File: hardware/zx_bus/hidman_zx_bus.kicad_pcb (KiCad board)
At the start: 2 copper layers, 99.1 x 40 mm, 31 parts, among them J1 X1A, J2 X1B, J3 UART, J4 Mini-DIN-6, J5 ISP, J6 Debug, J7 JTAG, J8 PS/2 External Bracket, U1 ATmega8A-A, U2 EPM3032ALC44, U3 AMS1117-3.3, U4 74LVC1G125DB

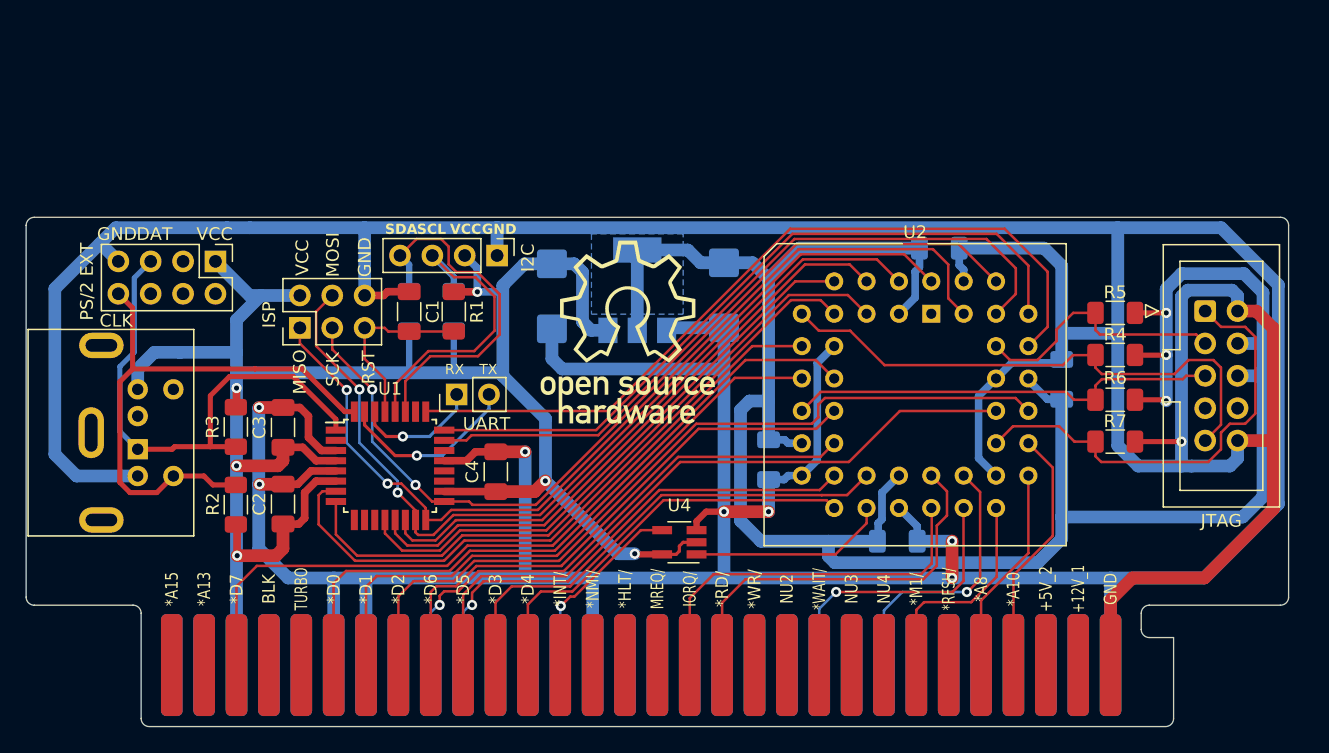
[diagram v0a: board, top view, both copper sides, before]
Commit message: Route ZX BUS card PCB.
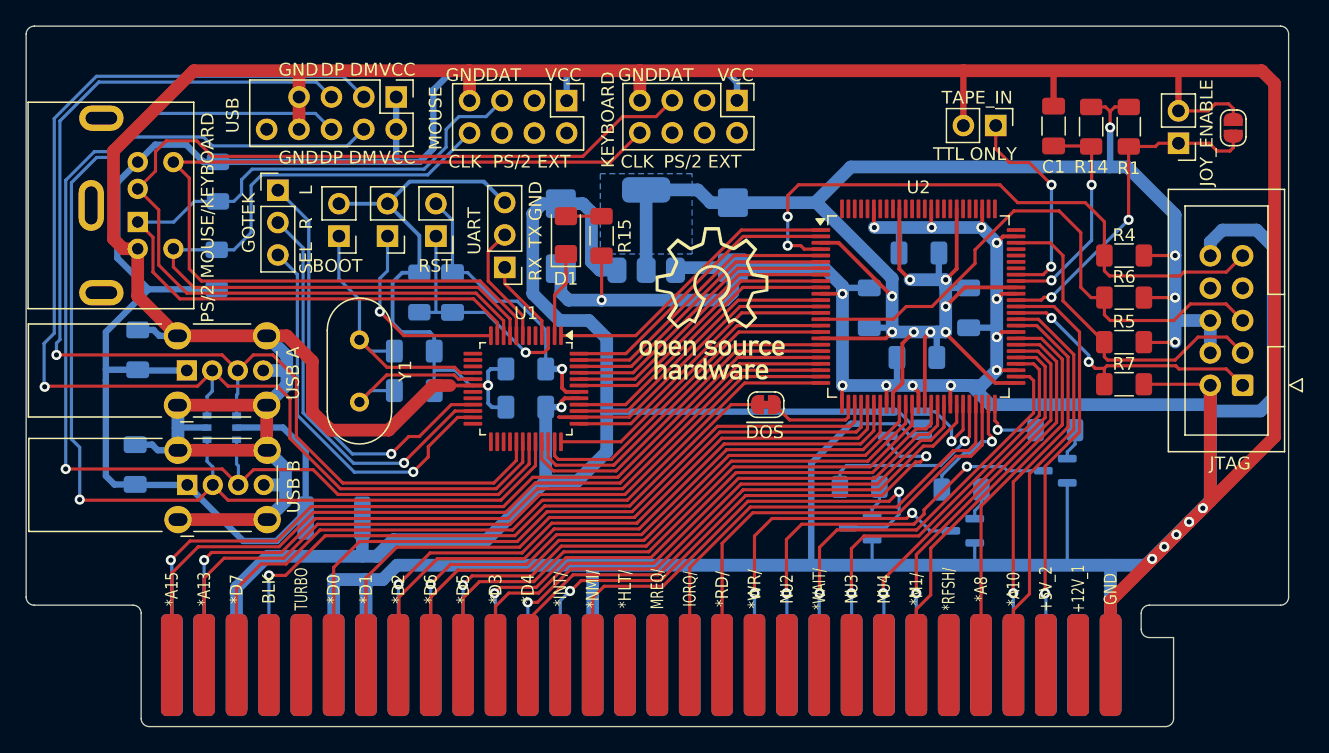
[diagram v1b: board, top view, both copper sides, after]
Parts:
- removed J6: Debug, Connector_PinHeader_2.54mm:PinHeader_1x04_P2.54mm_Vertical
- removed R8, R9: 2.2K, Resistor_SMD:R_1206_3216Metric_Pad1.30x1.75mm_HandSolder
- added C11: 0.1u, Capacitor_SMD:C_1206_3216Metric_Pad1.33x1.80mm_HandSolder, B.Cu at (112.6, 112.7)
- added C12: 0.1u, Capacitor_SMD:C_1206_3216Metric_Pad1.33x1.80mm_HandSolder, B.Cu at (116.5, 117.0)
- added C13: 0.1u, Capacitor_SMD:C_1206_3216Metric_Pad1.33x1.80mm_HandSolder, B.Cu at (112.4, 120.9)
- added C14: 0.1u, Capacitor_SMD:C_1206_3216Metric_Pad1.33x1.80mm_HandSolder, B.Cu at (108.7, 117.0)
- added D1: LED, LED_SMD:LED_1206_3216Metric_Pad1.42x1.75mm_HandSolder, F.Cu at (84.9, 111.3)
- added F2: Polyfuse, Fuse:Fuse_1812_4532Metric_Pad1.30x3.40mm_HandSolder, B.Cu at (66.7, 133.5)
- added J10: JOY_ENABLE, Connector_PinHeader_2.54mm:PinHeader_1x02_P2.54mm_Vertical, F.Cu at (133.0, 104.1)
- added J11: TAPE IN, Connector_PinHeader_2.54mm:PinHeader_1x02_P2.54mm_Vertical, F.Cu at (118.6, 102.7)
- added J12: USB EXT, Connector_PinHeader_2.54mm:PinHeader_2x05_P2.54mm_Vertical, F.Cu at (71.6, 100.5)
- added J13: PS/2 Mouse External Bracket, Connector_PinHeader_2.54mm:PinHeader_2x04_P2.54mm_Vertical, F.Cu at (85.0, 100.8)
- added J14: PS/2 Keyboard External Bracket, Connector_PinHeader_2.54mm:PinHeader_2x04_P2.54mm_Vertical, F.Cu at (98.3, 100.7)
- added J9: JTAG, Connector_IDC:IDC-Header_2x05_P2.54mm_Vertical, F.Cu at (138.0, 123.1)
- added JP1: SolderJumper_2_Bridged, Jumper:SolderJumper-2_P1.3mm_Bridged_RoundedPad1.0x1.5mm, F.Cu at (100.6, 124.6)
- added JP2: JOY_ENABLE, Jumper:SolderJumper-2_P1.3mm_Open_RoundedPad1.0x1.5mm, F.Cu at (137.3, 102.9)
- added Q1: BSS123, Package_TO_SOT_SMD:SOT-23, B.Cu at (116.0, 134.5)
- added Q2: BSS123, Package_TO_SOT_SMD:SOT-23, B.Cu at (108.0, 134.2)
- added Q3: BSS123, Package_TO_SOT_SMD:SOT-23, B.Cu at (123.3, 129.8)
- added R11: 1K, Resistor_SMD:R_1206_3216Metric_Pad1.30x1.75mm_HandSolder, B.Cu at (116.0, 131.3)
- added R12: 1K, Resistor_SMD:R_1206_3216Metric_Pad1.30x1.75mm_HandSolder, B.Cu at (108.0, 131.1)
- added R13: 1K, Resistor_SMD:R_1206_3216Metric_Pad1.30x1.75mm_HandSolder, B.Cu at (123.3, 126.6)
- added R14: 10K, Resistor_SMD:R_1206_3216Metric_Pad1.30x1.75mm_HandSolder, F.Cu at (126.1, 102.8)
- added R15: 1K, Resistor_SMD:R_1206_3216Metric_Pad1.30x1.75mm_HandSolder, F.Cu at (87.7, 111.4)
- added R16: 3.3K, Resistor_SMD:R_1206_3216Metric_Pad1.30x1.75mm_HandSolder, B.Cu at (57.5, 114.0)
- added SW1: RESET, Connector_PinHeader_2.54mm:PinHeader_1x02_P2.54mm_Vertical, F.Cu at (74.7, 111.4)
- added SW2: BOOT0, Connector_PinHeader_2.54mm:PinHeader_1x02_P2.54mm_Vertical, F.Cu at (67.1, 111.4)
- added SW3: BOOT1, Connector_PinHeader_2.54mm:PinHeader_1x02_P2.54mm_Vertical, F.Cu at (70.9, 111.4)
- added U6: IP4220CZ6, Package_SO:TSOP-6_1.65x3.05mm_P0.95mm, B.Cu at (57.9, 126.4)
- added Y1: 12MHz, Crystal:Crystal_HC49-4H_Vertical, F.Cu at (68.7, 124.4)
- C1: value 0.1u -> 0.1uF
- C2, C3: value 0.1u -> 22p; moved to B.Cu
- C4, U4: moved to B.Cu
- C5, C7, C8: value 0.1u -> 3.3u
- J3: footprint Connector_PinHeader_2.54mm:PinHeader_1x02_P2.54mm_Vertical -> Connector_PinHeader_2.54mm:PinHeader_1x03_P2.54mm_Vertical
- J4: value Mini-DIN-6 -> USB_A; footprint Connector_Mini-DIN_Female_6Pin:Connector_Mini-DIN_Female_6Pin_2rows -> Connector_USB:USB_A_Wuerth_614004134726_Horizontal
- J5: value ISP -> USB_A; footprint Connector_PinHeader_2.54mm:PinHeader_2x03_P2.54mm_Vertical -> Connector_USB:USB_A_Wuerth_614004134726_Horizontal
- J7: value JTAG -> Mouse / Key; footprint Connector_IDC:IDC-Header_2x05_P2.54mm_Vertical -> Connector_Mini-DIN_Female_6Pin:Connector_Mini-DIN_Female_6Pin_2rows
- J8: value PS/2 External Bracket -> GOTEK; footprint Connector_PinHeader_2.54mm:PinHeader_2x04_P2.54mm_Vertical -> Connector_PinHeader_2.54mm:PinHeader_1x03_P2.54mm_Vertical
- R1: value 2.2K -> 10K
- R2: value 4.7K -> 10K; moved to B.Cu
- R3: value 4.7K -> 3.3K; moved to B.Cu
- U1: value ATmega8A-A -> CH559L; footprint Package_QFP:TQFP-32_7x7mm_P0.8mm -> Package_QFP:LQFP-48_7x7mm_P0.5mm
- U2: value EPM3032ALC44 -> EPM3128ATC100; footprint Package_LCC:PLCC-44_THT-Socket -> Package_QFP:TQFP-100_14x14mm_P0.5mm
- moved J7 84.1 mm to (51.3, 110.3), turned to -90 degrees
- moved C7 60.1 mm to (51.1, 129.3), turned to 90 degrees
- moved R1 54.9 mm to (129.1, 102.8)
- moved C1 52.6 mm to (123.2, 102.7)
- moved C8 50.2 mm to (51.3, 120.3), turned to 90 degrees
- moved C5 42.1 mm to (81.8, 121.8), turned to 180 degrees
- moved C6 38.4 mm to (76.0, 115.8), turned to -90 degrees
- moved R2 22.0 mm to (73.4, 115.8), turned to 90 degrees
- moved U4 20.0 mm to (111.5, 126.1)
- moved R3 19.3 mm to (57.6, 107.1)
- moved C2 15.8 mm to (73.0, 120.4), turned to 0 degrees
- moved J5 15.2 mm to (55.2, 130.9), turned to 0 degrees
- moved U1 12.3 mm to (81.8, 123.3), turned to -90 degrees
- moved C3 10.7 mm to (73.0, 123.5), turned to 0 degrees
- moved J3 10.7 mm to (80.1, 113.8), turned to 180 degrees
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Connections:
- C1 pad 2: /RST -> /RST_IN
- C10 pad 1: /+3.3V -> +3.3V_CPLD
- C2 pad 1: VCC -> /P4_6
- C3 pad 1: VCC -> Net-(U1-P4.7/X0/SCK_)
- C4 pad 1: VCC -> +5V
- C5 pad 1: /+3.3V -> +3V3_MCU
- C6 pad 1: /+3.3V -> +3V3_MCU
- C6 pad 2: GND -> /RST
- C7 pad 1: /+3.3V -> +5V_FUSED
- C8 pad 1: /+3.3V -> +5V_FUSED
- C9 pad 1: VCC -> +5V
- J1 pad 3: VCC -> +5V
- J4 pad 1: /MDAT -> +5V_FUSED
- J4 pad 2: unconnected-(J4-Pad2) -> /DM_A
- J4 pad 3: GND -> /DP_A
- J4 pad 4: VCC -> GND
- J4 pad 5: /MCLK -> GND
- J5 pad 1: /DI4/MISO -> +5V_FUSED
- J5 pad 2: VCC -> /DM_B
- J5 pad 3: /DI5/SCK -> /DP_B
- J5 pad 4: /DI3/MOSI -> GND
- J5 pad 5: /RST -> GND
- J7 pad 1: /TCK -> /M_DAT
- J7 pad 2: GND -> /KEY_DAT
- J7 pad 3: /TDO -> GND
- J7 pad 4: /+3.3V -> +5V_FUSED
- J7 pad 5: /TMS -> /M_CLK
- J7 pad 6: /+3.3V -> /KEY_CLK
- J7 pad 7: unconnected-(J7-Pin_7-Pad7) -> (no net)
- J8 pad 1: VCC -> /LEFT
- J8 pad 2: unconnected-(J8-Pin_2-Pad2) -> /RIGHT
- J8 pad 3: unconnected-(J8-Pin_3-Pad3) -> /SELECT
- R1 pad 1: VCC -> +3.3V_CPLD
- R1 pad 2: /RST -> /JOY_ENABLE
- R2 pad 1: /MCLK -> /RST
- R2 pad 2: VCC -> GND
- R3 pad 1: /MDAT -> /M_DAT
- R3 pad 2: VCC -> +5V_FUSED
- R4 pad 2: /+3.3V -> +3.3V_CPLD
- R5 pad 2: /+3.3V -> +3.3V_CPLD
- R6 pad 2: /+3.3V -> +3.3V_CPLD
- U1 pad 1: /MDAT -> /JOY
- U1 pad 10: unconnected-(U1-PD6-Pad10) -> /KEY_DAT
- U1 pad 11: unconnected-(U1-PD7-Pad11) -> /M_DAT
- U1 pad 12: /DI0 -> /P3_6
- U1 pad 13: /DI1 -> /P3_7
- U1 pad 14: /DI2 -> /P4_3
- U1 pad 15: /DI3/MOSI -> /P4_2
- U1 pad 16: /DI4/MISO -> /P4_6
- U1 pad 17: /DI5/SCK -> Net-(U1-P4.7/X0/SCK_)
- U1 pad 18: VCC -> GND
- U1 pad 19: unconnected-(U1-ADC6-Pad19) -> /P4_1
- U1 pad 2: unconnected-(U1-PD4-Pad2) -> /P1_7
- U1 pad 20: unconnected-(U1-AREF-Pad20) -> /P4_0
- U1 pad 21: GND -> /LEFT
- U1 pad 22: unconnected-(U1-ADC7-Pad22) -> /RIGHT
- U1 pad 23: /MX -> /SELECT
- U1 pad 24: /MY -> /P2_3
- U1 pad 25: /MKEY -> /P2_4
- U1 pad 26: unconnected-(U1-PC3-Pad26) -> /P2_5
- U1 pad 27: /SDA -> /P2_6
- U1 pad 28: /SCL -> /P2_7
- U1 pad 29: /RST -> /DP_A
- U1 pad 3: GND -> /RST
- U1 pad 30: /RX -> /DM_A
- U1 pad 31: /TX -> /DP_B
- U1 pad 32: /MCLK -> /DM_B
- U1 pad 4: VCC -> /RX
- U1 pad 5: GND -> /P4_5
- U1 pad 6: VCC -> /P4_4
- U1 pad 7: /DI6 -> /TX
- U1 pad 8: /DI7 -> /KEY_CLK
- U1 pad 9: unconnected-(U1-PD5-Pad9) -> /M_CLK
- U2 pad 1: unconnected-(U2A-~{GCLR}-Pad1) -> /JOY
- U2 pad 10: GND -> /DI0
- U2 pad 11: /*D1 -> GND
- U2 pad 12: /*D0 -> /DI1
- U2 pad 13: /TMS -> /DI2
- U2 pad 14: /*D6 -> /DI3
- U2 pad 15: /+3.3V -> /TMS
- U2 pad 16: /*A0 -> /DI4
- U2 pad 17: GND -> /DI5
- U2 pad 18: /*D4 -> +3.3V_CPLD
- U2 pad 19: /*A1 -> /DI6
- U2 pad 2: /DI2 -> /STROBE
- U2 pad 20: /IORQGE/ -> /DI7
- U2 pad 21: /*D3 -> /*A14
- U2 pad 22: GND -> /*A15
- U2 pad 23: /+3.3V -> /*A12
- U2 pad 24: /*IORQ/ -> /*A13
- U2 pad 25: /*RD/ -> /*D7
- U2 pad 26: /*A7 -> GND
- U2 pad 27: /*A5 -> /DOS_IN
- U2 pad 28: /*M1/ -> /*D0
- U2 pad 29: /*A8 -> /*D1
- U2 pad 3: /+3.3V -> +3.3V_CPLD
- U2 pad 30: GND -> /CLK
- U2 pad 31: /*A10 -> /*D2
- U2 pad 32: /TCK -> /*A0
- U2 pad 33: /*D2 -> GND
- U2 pad 34: /*D5 -> +3.3V_CPLD
- U2 pad 35: /+3.3V -> /*D6
- U2 pad 36: GND -> /*A1
- U2 pad 37: /MKEY -> /*D5
- U2 pad 38: /TDO -> GND
- U2 pad 39: /MY -> +3.3V_CPLD
- U2 pad 4: /DI1 -> /TDI
- U2 pad 40: /DI5/SCK -> /*A2
- U2 pad 41: /MX -> /*D3
- U2 pad 42: GND -> /*A3
- U2 pad 43: /DI4/MISO -> GND
- U2 pad 44: /DI3/MOSI -> /*D4
- U2 pad 5: /DI7 -> /SCLK
- U2 pad 6: /DI0 -> /DAT
- U2 pad 7: /TDI -> /MKEY
- U2 pad 8: /DI6 -> /MY
- U2 pad 9: /*D7 -> /MX
- U3 pad 2: /+3.3V -> +3.3V_CPLD
- U3 pad 3: VCC -> +5V
- U4 pad 2: VCC -> +5V
- U4 pad 5: VCC -> +5V
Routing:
- net /+3.3V: track 176.1 -> 0.00 mm, vias 3 -> 0
- net +3.3V_CPLD: track 0.00 -> 163.0 mm, vias 0 -> 12
- net VCC: track 160.8 -> 0.00 mm, vias 6 -> 0
- net +5V_FUSED: track 0.00 -> 132.2 mm
- net GND: track 505.7 -> 618.9 mm, vias 8 -> 19
- net +5V: track 0.00 -> 110.4 mm, vias 0 -> 1
- net /DM_A: track 0.00 -> 97.7 mm, vias 0 -> 1
- net /DM_B: track 0.00 -> 93.9 mm, vias 0 -> 1
- net /DP_A: track 0.00 -> 91.2 mm, vias 0 -> 1
- net /DP_B: track 0.00 -> 90.7 mm, vias 0 -> 1
- net /KEY_DAT: track 0.00 -> 83.5 mm
- net /KEY_CLK: track 0.00 -> 75.1 mm
- net /DI4/MISO: track 74.5 -> 0.00 mm, vias 2 -> 0
- net /DI3/MOSI: track 72.9 -> 0.00 mm, vias 2 -> 0
- net /DI5/SCK: track 71.1 -> 0.00 mm, vias 2 -> 0
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- added copper zone on B.Cu, net +3.3V_CPLD
- removed copper zone on B.Cu, net /+3.3V
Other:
- board size 99.1 x 40 mm -> 99.1 x 55 mm
- board text added: "BOOT"
- board text added: "DM"
- board text added: "DP"
- board text added: "GOTEK"
- board text added: "JOY_ENABLE"
- board text added: "KEYBOARD"
- board text added: "L"
- board text added: "MOUSE"
- board text added: "PS/2 MOUSE/KEYBOARD"
- board text added: "R"
- board text added: "SEL"
- board text added: "TAPE_IN"
- board text added: "TTL ONLY"
- board text added: "USB"
- board text added: "USB A"
- board text added: "USB B"
- board text added: "V.1.0"
- board text added: "ZX BUS USB / PS/2 Input Controller"
- board text added: "~{DOS}"
- board text removed: "I2C"
- board text removed: "ISP"
- board text removed: "MISO"
- board text removed: "MOSI"
- board text removed: "SCK"
- board text removed: "SCL"
- board text removed: "SDA"
- board text removed: "ZX BUS Kempston Mouse Controller"

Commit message: Remove BOOT1 switch from schematic. Correct LED polarity.
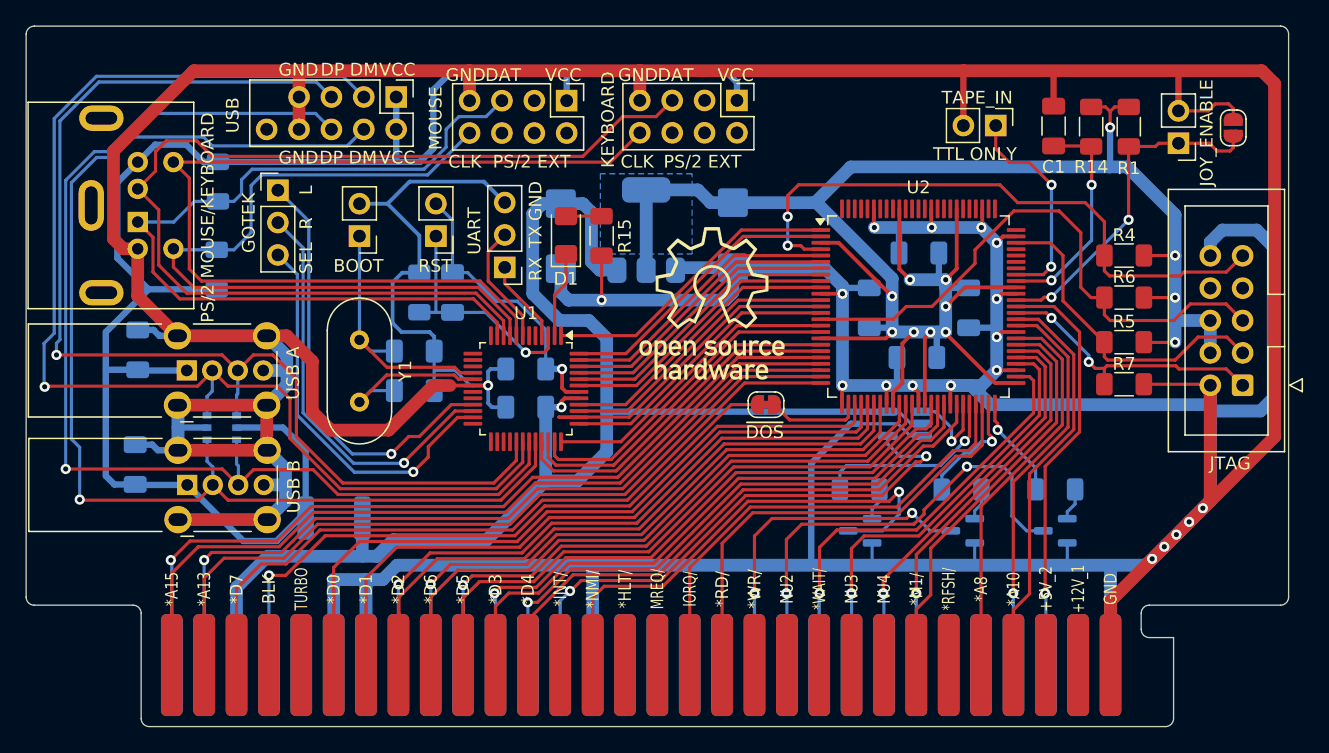
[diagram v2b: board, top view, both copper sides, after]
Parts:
- removed SW3: BOOT1, Connector_PinHeader_2.54mm:PinHeader_1x02_P2.54mm_Vertical
- moved Q3 4.71 mm to (123.3, 134.5)
- moved R13 4.65 mm to (123.3, 131.2)
- moved SW2 1.61 mm to (68.7, 111.4)
- moved Q2 0.25 mm to (108.0, 134.5)
- moved R12 0.20 mm to (108.0, 131.2)
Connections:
- D1 pad 1: /P1_7 -> Net-(D1-K)
- D1 pad 2: Net-(D1-A) -> /P1_7
- R15 pad 1: Net-(D1-A) -> Net-(D1-K)
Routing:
- net /P3_6: track 15.7 -> 0.00 mm, vias 1 -> 0
- net GND: track 618.9 -> 612.3 mm
- net /*RST/: track 32.7 -> 36.6 mm
- net /RST_OUT: track 5.09 -> 8.01 mm
- net Net-(D1-A): track 2.80 -> 0.00 mm
- net /P1_7: track 6.77 -> 9.57 mm
- net /P4_6: track 21.9 -> 21.2 mm

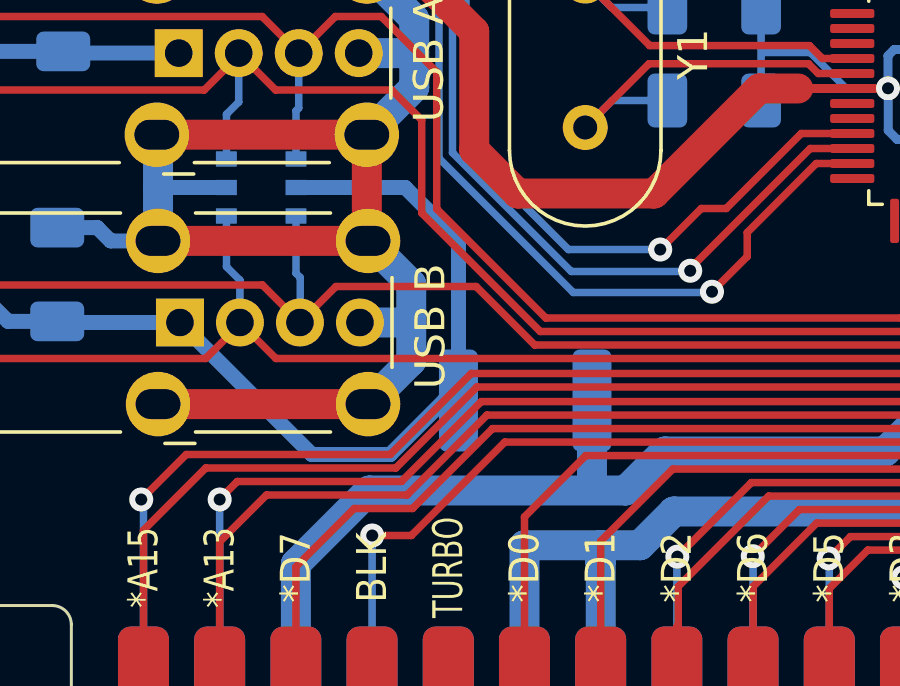
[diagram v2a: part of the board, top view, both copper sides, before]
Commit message: Replace 1812 polyfuse Littelfuse 1812L050PR (0.5A, 15V) with 1206 Bourns MF-NSMF075-2 (0.75A, 6V). Add schematic comments about CH559L omitted reset and external clock components.
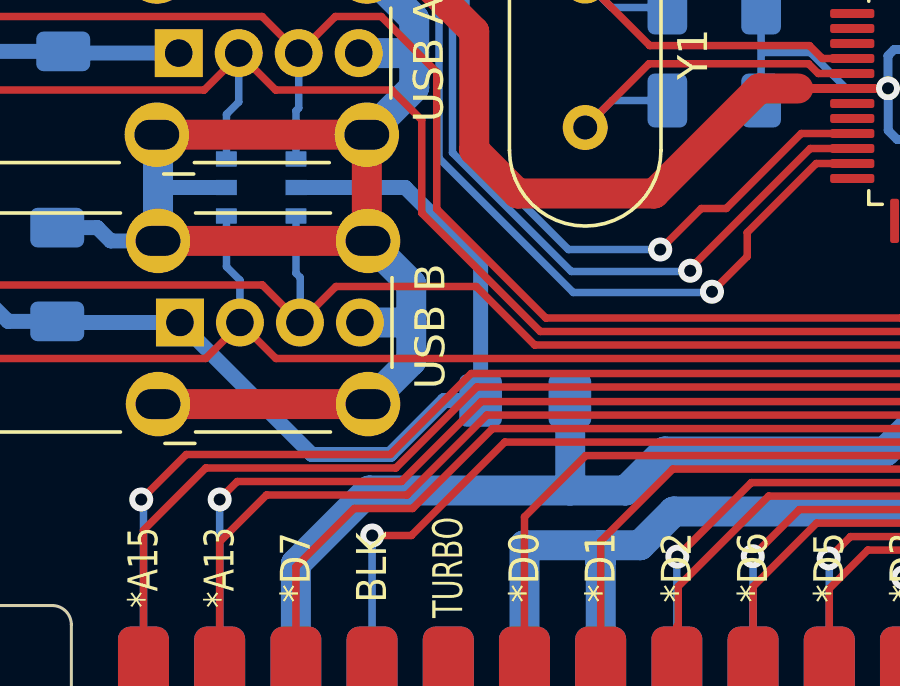
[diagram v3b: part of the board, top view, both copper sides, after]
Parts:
- F2: value Polyfuse -> MF-NSMF075-2; footprint Fuse:Fuse_1812_4532Metric_Pad1.30x3.40mm_HandSolder -> Fuse:Fuse_1206_3216Metric_Pad1.42x1.75mm_HandSolder
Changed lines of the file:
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@@
 		)
 	)
-	(footprint "Fuse:Fuse_1812_4532Metric_Pad1.30x3.40mm_HandSolder"
+	(footprint "Fuse:Fuse_1206_3216Metric_Pad1.42x1.75mm_HandSolder"
 		(layer "B.Cu")
 		(at 66.7 133.5 180)
-		(descr "Fuse SMD 1812 (4532 Metric), square (rectangular) end terminal, IPC_7351 nominal with elongated pad for handsoldering. (Body size source: https://www.nikhef.nl/pub/departments/mt/projects/detectorR_D/dtddice/ERJ2G.pdf), generated with kicad-footprint-generator")
+		(descr "Fuse SMD 1206 (3216 Metric), square (rectangular) end terminal, IPC_7351 nominal with elongated pad for handsoldering. (Body size source: http://www.tortai-tech.com/upload/download/2011102023233369053.pdf), generated with kicad-footprint-generator")
 		(tags "fuse handsolder")
 		(property "Reference" "F2"
-			(at 0 2.65 180)
+			(at 0 1.82 180)
 			(layer "B.SilkS")
 			(effects
@@
 			)
 		)
-		(property "Value" "Polyfuse"
-			(at 0 -2.65 180)
+		(property "Value" "MF-NSMF075-2"
+			(at 0 -1.82 180)
 			(layer "B.Fab")
 			(effects
@@
 			)
 		)
-		(property "Footprint" "Fuse:Fuse_1812_4532Metric_Pad1.30x3.40mm_HandSolder"
+		(property "Footprint" "Fuse:Fuse_1206_3216Metric_Pad1.42x1.75mm_HandSolder"
 			(at 0 0 0)
 			(unlocked yes)
@@
 		(attr smd)
 		(fp_line
-			(start 1.386252 1.71)
-			(end -1.386252 1.71)
+			(start 0.602064 0.91)
+			(end -0.602064 0.91)
 			(stroke
 				(width 0.12)
@@
 		)
 		(fp_line
-			(start 1.386252 -1.71)
-			(end -1.386252 -1.71)
+			(start 0.602064 -0.91)
+			(end -0.602064 -0.91)
 			(stroke
 				(width 0.12)
@@
 		)
 		(fp_line
-			(start 3.12 1.95)
-			(end -3.12 1.95)
+			(start 2.45 1.12)
+			(end -2.45 1.12)
 			(stroke
 				(width 0.05)
@@
 		)
 		(fp_line
-			(start 3.12 -1.95)
-			(end 3.12 1.95)
+			(start 2.45 -1.12)
+			(end 2.45 1.12)
 			(stroke
 				(width 0.05)
@@
 		)
 		(fp_line
-			(start -3.12 1.95)
-			(end -3.12 -1.95)
+			(start -2.45 1.12)
+			(end -2.45 -1.12)
 			(stroke
 				(width 0.05)
@@
 		)
 		(fp_line
-			(start -3.12 -1.95)
-			(end 3.12 -1.95)
+			(start -2.45 -1.12)
+			(end 2.45 -1.12)
 			(stroke
 				(width 0.05)
@@
 		)
 		(fp_line
-			(start 2.25 1.6)
-			(end -2.25 1.6)
+			(start 1.6 0.8)
+			(end -1.6 0.8)
 			(stroke
 				(width 0.1)
@@
 		)
 		(fp_line
-			(start 2.25 -1.6)
-			(end 2.25 1.6)
+			(start 1.6 -0.8)
+			(end 1.6 0.8)
 			(stroke
 				(width 0.1)
@@
 		)
 		(fp_line
-			(start -2.25 1.6)
-			(end -2.25 -1.6)
+			(start -1.6 0.8)
+			(end -1.6 -0.8)
 			(stroke
 				(width 0.1)
@@
 		)
 		(fp_line
-			(start -2.25 -1.6)
-			(end 2.25 -1.6)
+			(start -1.6 -0.8)
+			(end 1.6 -0.8)
 			(stroke
 				(width 0.1)
@@
 			(effects
 				(font
-					(size 1 1)
-					(thickness 0.15)
+					(size 0.8 0.8)
+					(thickness 0.12)
 				)
 				(justify mirror)
@@
 		)
 		(pad "1" smd roundrect
-			(at -2.225 0 180)
-			(size 1.3 3.4)
+			(at -1.4875 0 180)
+			(size 1.425 1.75)
 			(layers "B.Cu" "B.Paste" "B.Mask")
-			(roundrect_rratio 0.192308)
+			(roundrect_rratio 0.175439)
 			(net 76 "+5V")
 			(pintype "passive")
 		)
 		(pad "2" smd roundrect
-			(at 2.225 0 180)
-			(size 1.3 3.4)
+			(at 1.4875 0 180)
+			(size 1.425 1.75)
 			(layers "B.Cu" "B.Paste" "B.Mask")
-			(roundrect_rratio 0.192308)
+			(roundrect_rratio 0.175439)
 			(net 156 "+5V_FUSED")
 			(pintype "passive")
 		)
-		(model "${KICAD8_3DMODEL_DIR}/Fuse.3dshapes/Fuse_1812_4532Metric.wrl"
+		(model "${KICAD8_3DMODEL_DIR}/Fuse.3dshapes/Fuse_1206_3216Metric.wrl"
 			(offset
 				(xyz 0 0 0)
@@
 	)
 	(segment
+		(start 68.2 133.5125)
+		(end 68.2 136.5)
+		(width 1)
+		(layer "B.Cu")
+		(net 76)
+	)
+	(segment
 		(start 87.55 114.05)
 		(end 86.9 113.4)
@@
 	)
 	(segment
-		(start 68.925 133.5)
-		(end 68.925 136.475)
-		(width 1)
-		(layer "B.Cu")
-		(net 76)
-	)
-	(segment
 		(start 110.15 125.15)
 		(end 88.1 125.15)
@@
 	)
 	(segment
+		(start 68.1875 133.5)
+		(end 68.2 133.5125)
+		(width 1)
+		(layer "B.Cu")
+		(net 76)
+	)
+	(segment
 		(start 88.9 114.05)
 		(end 87.55 114.05)
@@
 	)
 	(segment
-		(start 64.475 133.5)
-		(end 64.475 128.175)
+		(start 59.06 126.4)
+		(end 62.7 126.4)
 		(width 0.5)
 		(layer "B.Cu")
@@
 	)
 	(segment
-		(start 64.475 128.175)
-		(end 62.7 126.4)
+		(start 65.2125 128.9125)
+		(end 65.2125 133.5)
 		(width 0.5)
 		(layer "B.Cu")
@@
 	(segment
 		(start 62.7 126.4)
-		(end 59.06 126.4)
+		(end 65.2125 128.9125)
 		(width 0.5)
 		(layer "B.Cu")
